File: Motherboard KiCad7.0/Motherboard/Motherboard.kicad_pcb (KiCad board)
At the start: 2 copper layers, 83.8 x 83.8 mm, 85 parts, among them J1 USB_B_Micro, J10 SWD_01x04_Pin, J11 430450200, J12 430450200, J13 430450200, J14 430450200, J15 430450200, J2 B04B-XASK-1, J3 430450200, J4 430450200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

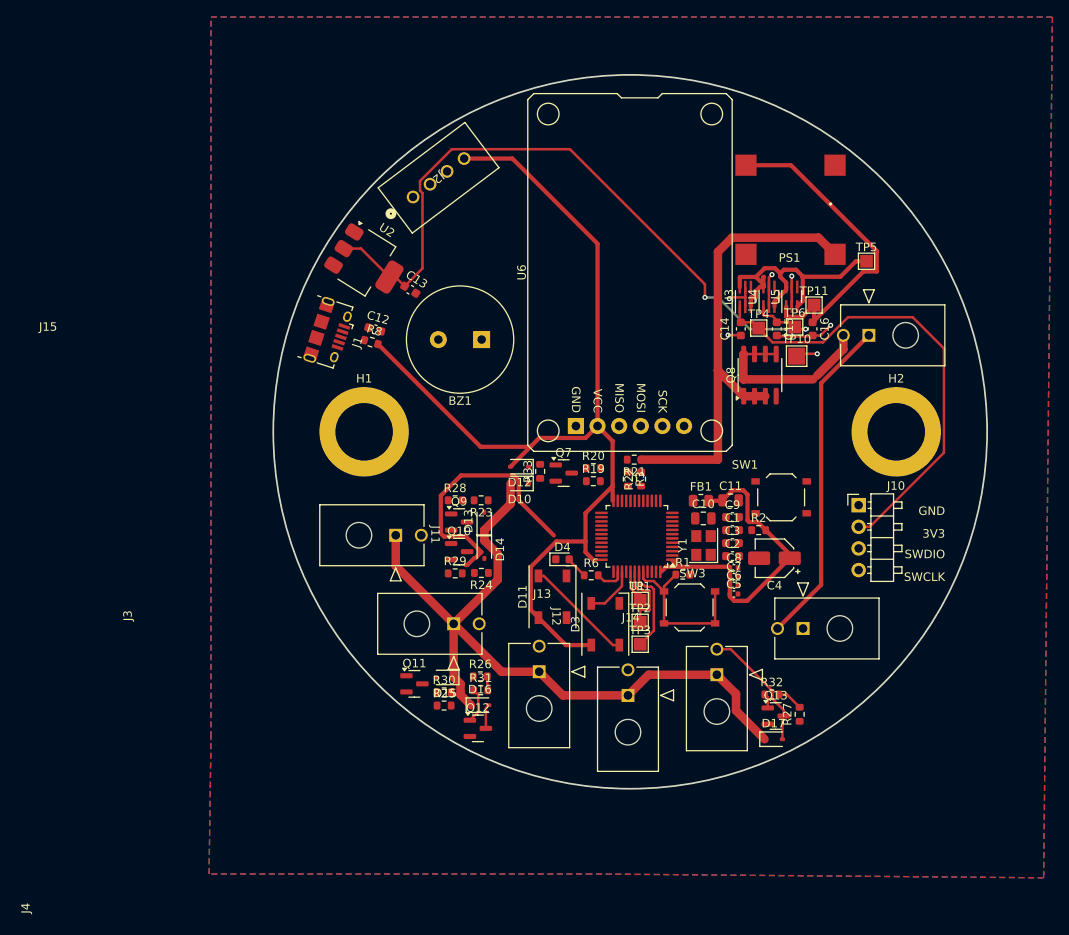
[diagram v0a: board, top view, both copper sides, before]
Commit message: Started wiring signal traces
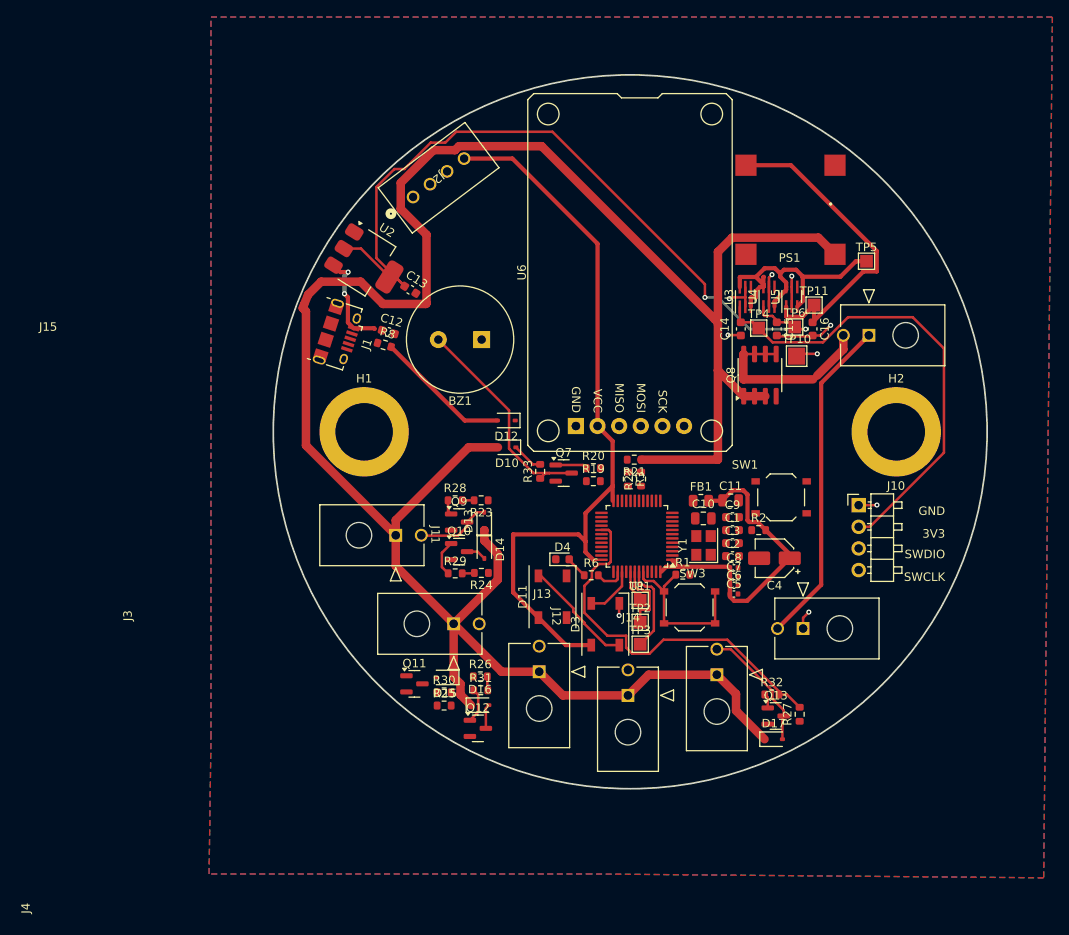
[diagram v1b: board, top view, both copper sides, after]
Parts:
- moved D12 5.64 mm to (177.5, 121.6)
- moved D10 4.50 mm to (177.6, 124.7)
- moved C12 1.62 mm to (163.6, 111.2)
- moved R8 1.58 mm to (163.2, 112.7)
- moved J1 1.12 mm to (157.8, 111.5)
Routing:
- net +BATT: track 144.9 -> 266.9 mm
- net Pump: track 3.07 -> 44.9 mm
- net (no net): track 31.1 -> 0.00 mm
- net Net-(BZ1--): track 0.00 -> 26.1 mm
- net +3.3V: track 188.2 -> 175.1 mm
- net /USB_5V: track 0.00 -> 11.8 mm, vias 0 -> 2
- net Net-(D13-A): track 0.00 -> 8.86 mm
- net V_REGUSB: track 85.5 -> 92.3 mm
- net GND: track 22.7 -> 28.5 mm, vias 6 -> 9
- net Net-(Q10-G): track 0.00 -> 4.26 mm
- net Net-(Q7-G): track 0.00 -> 3.76 mm
- net Net-(BZ1-+): track 0.00 -> 3.68 mm
- net Net-(D14-A): track 0.00 -> 2.36 mm
- net Net-(Q9-G): track 0.00 -> 1.75 mm
- net Sol_1: track 0.00 -> 1.45 mm
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
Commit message: motherboard pcb layout - Mohamad
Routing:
- net MUX_SCL: track 0.00 -> 50.6 mm, vias 0 -> 2
- net USB_D+: track 0.00 -> 49.0 mm
- net MUX_SDA: track 0.00 -> 46.7 mm, vias 0 -> 1
- net GND: track 28.5 -> 58.5 mm, vias 9 -> 13
- net Sol_0: track 1.41 -> 29.4 mm, vias 0 -> 2
- net Net-(D16-A): track 2.87 -> 23.2 mm, vias 0 -> 2
- net +3.3V: track 175.1 -> 195.0 mm, vias 0 -> 2
- net SD_MISO: track 0.00 -> 14.2 mm
- net Net-(BZ1-+): track 3.68 -> 17.8 mm
- net +3.3VA: track 0.00 -> 13.1 mm
- net SD_CS: track 0.00 -> 10.1 mm
- net SD_CLK: track 0.00 -> 9.11 mm
- net SD_MOSI: track 0.00 -> 8.82 mm
- net BATT_SENSE: track 0.00 -> 5.61 mm
- net BOOT1: track 0.00 -> 1.87 mm

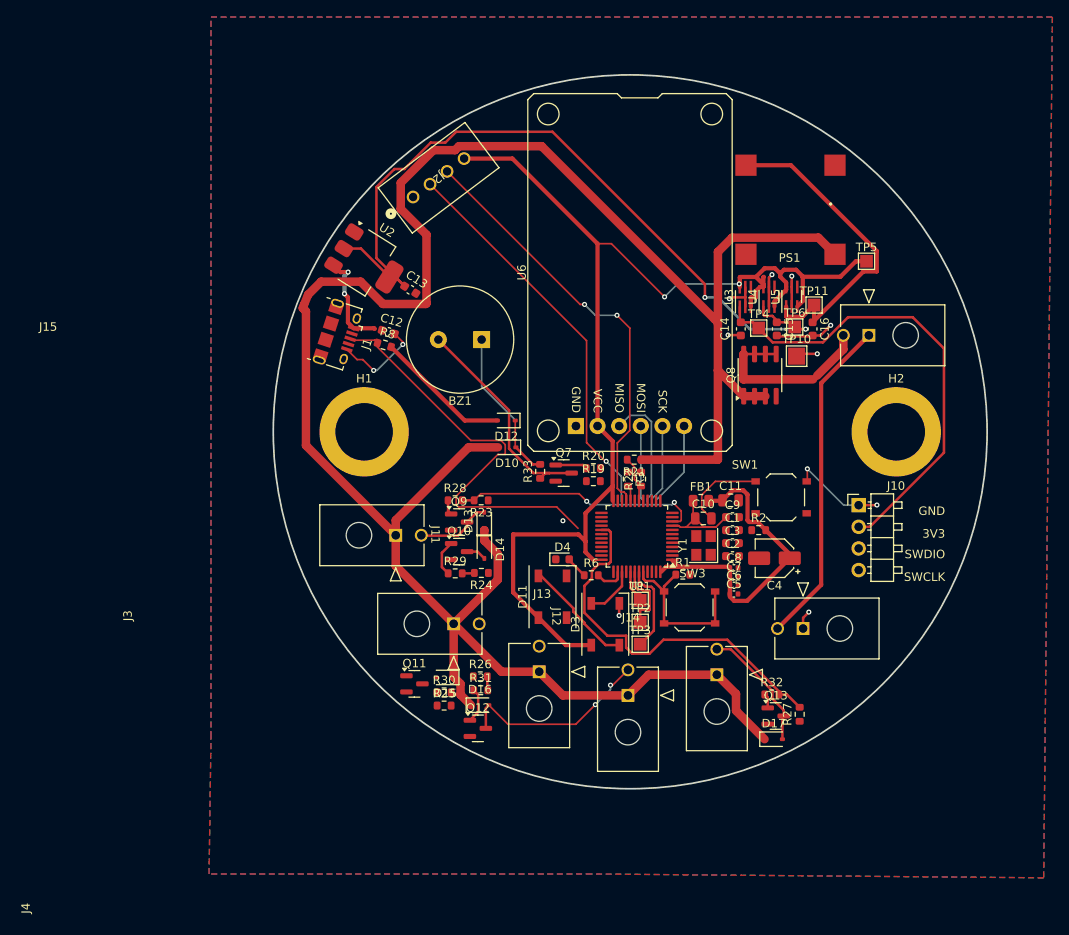
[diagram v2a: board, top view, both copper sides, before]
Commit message: Layout v2
Redid layout with new sensors added. Very tight so might need a v3
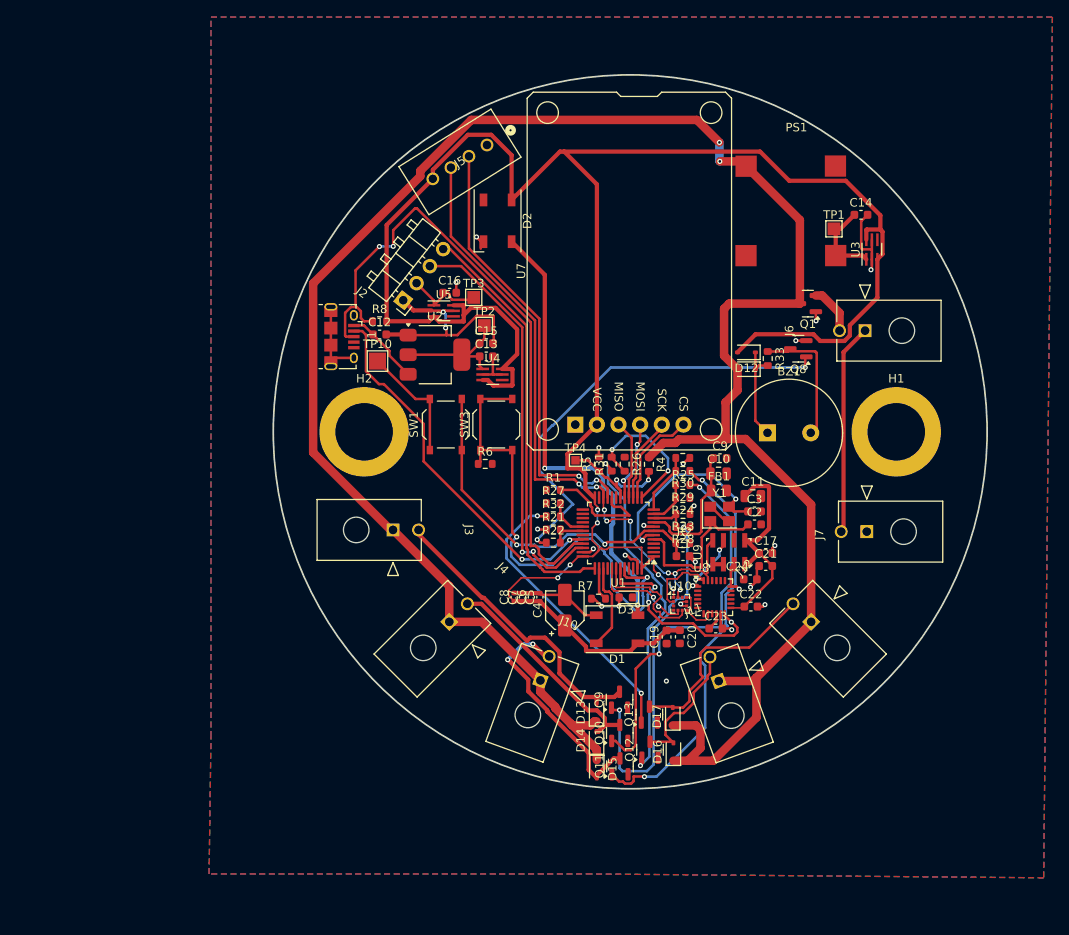
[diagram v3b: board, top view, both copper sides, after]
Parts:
- removed D11: WS2812B, LED_SMD:LED_WS2812B_PLCC4_5.0x5.0mm_P3.2mm
- removed D4: DB_LED (YLW), LED_SMD:LED_0603_1608Metric
- removed J13, J14, J15: 430450200, CONN 0430450200:CON_430450200_MOL
- removed Q7: AO3400A, Package_TO_SOT_SMD:SOT-23
- removed R19: 10k, Resistor_SMD:R_0603_1608Metric
- removed R20: 510R, Resistor_SMD:R_0603_1608Metric
- removed R3: 100k, Resistor_SMD:R_0603_1608Metric
- removed TP11: TP_VBUCK, TestPoint:TestPoint_Pad_1.5x1.5mm
- removed TP5: TP_MUX, TestPoint:TestPoint_Pad_1.5x1.5mm
- removed TP6: TP_VUSB, TestPoint:TestPoint_Pad_1.5x1.5mm
- removed U6: Micro_SD_Reader, MicroSD Card Reader:MicroSD Card Reader
- added C17: 100nF, Capacitor_SMD:C_0603_1608Metric, F.Cu at (208.0, 137.1)
- added C19: 100nF, Capacitor_SMD:C_0603_1608Metric, F.Cu at (196.3, 147.0)
- added C20: 100nF, Capacitor_SMD:C_0603_1608Metric, F.Cu at (197.9, 147.0)
- added C21: 10nF, Capacitor_SMD:C_0603_1608Metric, F.Cu at (208.0, 138.7)
- added C22: 100nF, Capacitor_SMD:C_0603_1608Metric, F.Cu at (206.2, 143.4)
- added C23: 100nF, Capacitor_SMD:C_0603_1608Metric, F.Cu at (202.1, 146.0)
- added C24: 2.2nF, Capacitor_SMD:C_0603_1608Metric, F.Cu at (206.2, 140.2)
- added D1: WS2812B, LED_SMD:LED_WS2812B_PLCC4_5.0x5.0mm_P3.2mm, F.Cu at (190.5, 146.1)
- added D2: WS2812B, LED_SMD:LED_WS2812B_PLCC4_5.0x5.0mm_P3.2mm, F.Cu at (176.5, 98.1)
- added J5: B04B-XASK-1, B04B_XASK_1:CONN_B04B-XASK-1_JST, F.Cu at (175.2, 89.2)
- added J6: 430450200, CONN 0430450200:CON_430450200_MOL, F.Cu at (219.6, 111.0)
- added J7: 430450200, CONN 0430450200:CON_430450200_MOL, F.Cu at (219.8, 134.6)
- added Q1: AO4447A, Package_TO_SOT_SMD:SOT-23, F.Cu at (212.9, 107.8)
- added R4: 30k, Resistor_SMD:R_0603_1608Metric, F.Cu at (194.2, 126.7)
- added R5: 10k, Resistor_SMD:R_0603_1608Metric, F.Cu at (188.4, 126.7)
- added R7: 560, Resistor_SMD:R_0603_1608Metric, F.Cu at (188.3, 142.5)
- added U10: KX134-1211, Package_LGA:LGA-12_2x2mm_P0.5mm, F.Cu at (197.9, 143.1)
- added U7: Micro_SD_Reader, MicroSD Card Reader:MicroSD Card Reader, F.Cu at (191.9, 104.0)
- added U8: MPU-6050, Sensor_Motion:InvenSense_QFN-24_4x4mm_P0.5mm, F.Cu at (201.9, 142.3)
- added U9: MS560702BA03-50, MS5607_Handsolder:MS5607_Handsolder, F.Cu at (203.6, 137.1)
- C4: value 10uF -> 10u
- D3: value WS2812B -> LED; footprint LED_SMD:LED_WS2812B_PLCC4_5.0x5.0mm_P3.2mm -> LED_SMD:LED_0603_1608Metric
- J10: value SWD_01x04_Pin -> 430450200; footprint SWD_Header:SWD_PinHeader_1x04_P2.54mm_Horizontal -> CONN 0430450200:CON_430450200_MOL
- J2: value B04B-XASK-1 -> SWD_01x04_Pin; footprint B04B_XASK_1:CONN_B04B-XASK-1_JST -> SWD_Header:SWD_PinHeader_1x04_P2.54mm_Horizontal
- PS1: footprint CONV_K7812JT-500R3-LB:CONV_K7812JT-500R3-LB -> K7805JT_500R3:K78_JT-500R3_MNS
- Q8: value AO4447A -> AO3400A; footprint Package_SO:SOIC-8_3.9x4.9mm_P1.27mm -> Package_TO_SOT_SMD:SOT-23
- R21: value 30k -> 10k
- R22: value 10k -> 510R
- R6: value 560 -> 100k
- TP1: value TP_PB5 -> TP_VBUCK
- TP2: value TP_PB6 -> TP_VREGUSB
- TP3: value TP_PB7 -> TP_VSWD
- TP4: value TP_VSWD -> TestPoint; footprint TestPoint:TestPoint_Pad_1.5x1.5mm -> TestPoint:TestPoint_Pad_1.0x1.0mm
- moved H1 62.5 mm to (223.3, 122.9)
- moved H2 62.5 mm to (160.8, 122.9)
- moved J3 60.4 mm to (164.2, 134.4), turned to -90 degrees
- moved TP10 49.2 mm to (162.4, 114.6)
- moved TP1 49.2 mm to (216.0, 99.1)
- moved TP3 45.2 mm to (173.7, 107.1)
- moved C16 42.8 mm to (170.8, 106.6), turned to 0 degrees
- moved J10 42.7 mm to (181.5, 152.1), turned to -20 degrees
- moved J12 42.0 mm to (213.3, 145.2), turned to 45 degrees
- moved J11 41.6 mm to (202.4, 152.2), turned to 20 degrees
- moved J4 41.6 mm to (170.8, 145.2), turned to -45 degrees
- moved U5 40.9 mm to (170.2, 108.7), turned to 0 degrees
- moved R25 40.4 mm to (198.2, 126.0), turned to 180 degrees
- moved SW1 40.3 mm to (170.4, 122.0), turned to 90 degrees
- moved TP2 39.4 mm to (174.9, 110.4)
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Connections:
- C14 pad 1: V_SWD -> V_BUCK
- C16 pad 1: V_Buck -> V_SWD
- D3 pad 1: +3.3V -> GND
- J10 pad 1: GND -> +BATT
- J10 pad 2: V_SWD -> Net-(D15-A)
- J11 pad 2: Net-(D13-A) -> Net-(D16-A)
- J12 pad 2: Net-(D14-A) -> Net-(D17-A)
- J2 pad 2: MUX_SDA -> V_SWD
- J2 pad 3: MUX_SCL -> SWDIO
- J2 pad 4: +3.3V -> SWCLK
- J3 pad 1: Net-(J3-Pad1) -> +BATT
- J3 pad 2: Net-(J3-Pad2) -> Net-(D13-A)
- J4 pad 1: GND -> +BATT
- J4 pad 2: Net-(J3-Pad1) -> Net-(D14-A)
- PS1 pad 3: V_Buck -> V_BUCK
- Q8 pad 1: +BATT -> Net-(Q8-G)
- Q8 pad 2: +BATT -> GND
- Q8 pad 3: +BATT -> Net-(BZ1--)
- R1 pad 1: BOOT0 -> GND
- R1 pad 2: GND -> BOOT1
- R21 pad 1: +BATT -> GND
- R21 pad 2: BATT_SENSE -> BUZZER
- R22 pad 1: BATT_SENSE -> Net-(Q8-G)
- R22 pad 2: GND -> BUZZER
- R6 pad 1: Net-(D4-A) -> BOOT0
- R6 pad 2: DB_LED -> GND
- TP1 pad 1: Net-(U1-PB5) -> V_BUCK
- TP2 pad 1: Net-(U1-PB6) -> V_REGUSB
- TP3 pad 1: Net-(U1-PB7) -> V_SWD
- TP4 pad 1: V_SWD -> BATT_SENSE
- U1 pad 21: MUX_SCL -> SDA
- U1 pad 22: MUX_SDA -> SCL
- U1 pad 41: Net-(U1-PB5) -> ACCEL_INT1
- U1 pad 42: Net-(U1-PB6) -> ACCEL_INT2
- U1 pad 43: Net-(U1-PB7) -> GYRO_INT
- U3 pad 1: V_SWD -> V_BUCK
- U5 pad 1: V_Buck -> V_SWD
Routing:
- net +3.3V: track 195.0 -> 292.1 mm, vias 2 -> 6
- net SCL: track 0.00 -> 77.4 mm, vias 0 -> 8
- net V_REGUSB: track 92.3 -> 15.1 mm, vias 2 -> 0
- net SDA: track 0.00 -> 66.1 mm, vias 0 -> 4
- net Net-(D1-DOUT): track 0.00 -> 53.6 mm, vias 0 -> 2
- net Net-(Q8-G): track 0.00 -> 52.5 mm, vias 0 -> 2
- net MUX_SCL: track 50.6 -> 0.00 mm, vias 2 -> 0
- net SWCLK: track 0.00 -> 49.4 mm
- net SWDIO: track 0.00 -> 49.4 mm, vias 0 -> 2
- net Net-(Q11-G): track 0.00 -> 49.1 mm, vias 0 -> 2
- net MUX_SDA: track 46.7 -> 0.00 mm, vias 1 -> 0
- net V_SWD: track 55.3 -> 9.61 mm
- net USB_D-: track 0.00 -> 44.0 mm, vias 0 -> 2
- net STM_RESET: track 0.00 -> 42.4 mm, vias 0 -> 2
- net Net-(Q9-G): track 1.75 -> 43.2 mm, vias 0 -> 2
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
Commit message: Finished layout and added some part numbers
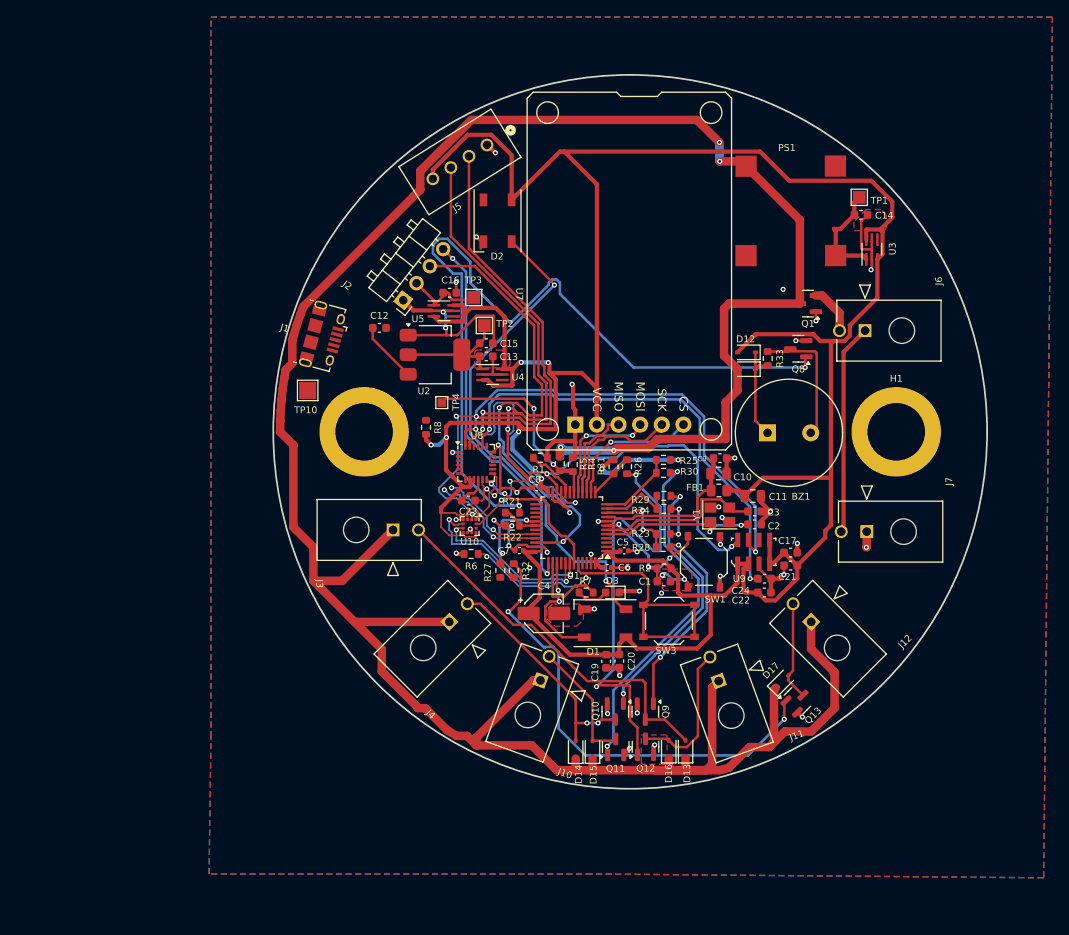
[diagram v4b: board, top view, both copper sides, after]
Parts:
- moved SW1 34.3 mm to (200.7, 138.2), turned to -90 degrees
- moved C23 32.7 mm to (173.1, 131.0)
- moved U8 32.1 mm to (173.9, 126.5)
- moved SW3 30.7 mm to (196.6, 145.1), turned to 0 degrees
- moved U10 26.3 mm to (173.2, 134.0), turned to -90 degrees
- moved Q13 17.5 mm to (211.7, 154.5), turned to 45 degrees
- moved TP4 17.1 mm to (169.9, 119.5)
- moved R8 13.6 mm to (168.1, 122.4), turned to -90 degrees
- moved D17 13.5 mm to (209.9, 152.2), turned to 45 degrees
- moved C8 13.1 mm to (181.1, 129.5), turned to 180 degrees
- moved D13 11.3 mm to (198.6, 160.2)
- moved C5 11.3 mm to (191.3, 136.9), turned to 0 degrees
- moved R6 10.7 mm to (173.4, 137.2), turned to 180 degrees
- moved R4 10.5 mm to (183.8, 126.7)
- moved R27 10.0 mm to (176.8, 139.2), turned to 90 degrees
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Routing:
- net +3.3V: track 292.1 -> 377.8 mm
- net SDA: track 66.1 -> 144.0 mm, vias 4 -> 6
- net USB_D+: track 77.5 -> 14.1 mm
- net +BATT: track 257.5 -> 315.2 mm, vias 2 -> 4
- net Net-(U8-CPOUT): track 0.00 -> 53.8 mm, vias 0 -> 2
- net GND: track 96.7 -> 150.1 mm, vias 23 -> 50
- net Net-(Q8-G): track 52.5 -> 96.1 mm
- net USB_D-: track 44.0 -> 13.1 mm
- net SCL: track 77.4 -> 107.5 mm
- net Net-(Q13-G): track 33.9 -> 55.7 mm
- net STM_RESET: track 42.4 -> 22.1 mm, vias 2 -> 5
- net Net-(Q9-G): track 43.2 -> 23.7 mm
- net Net-(Q10-G): track 45.5 -> 31.5 mm
- net Net-(D15-A): track 28.3 -> 14.8 mm, vias 2 -> 0
- net Net-(D17-A): track 24.8 -> 11.7 mm
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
